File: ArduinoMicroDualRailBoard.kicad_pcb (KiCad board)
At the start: 2 copper layers, 54 parts, among them J1 Conn_01x20_Male, J2 Screw_Terminal_01x03, J3 Conn_01x20_Male, J4 Conn_01x20_Male, J5 Screw_Terminal_01x03, J6 Conn_01x20_Male, J7 SDS-50J, J8 SDS-50J, U1 L7805, U2 L7815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

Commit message: Initial PCB layout
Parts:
- moved F3 108.9 mm to (181.0, 108.6), turned to 90 degrees
- moved U8 100.3 mm to (173.4, 74.3), turned to 180 degrees
- moved R2 95.8 mm to (90.8, 125.1), turned to 270 degrees
- moved C6 92.7 mm to (203.8, 88.9), turned to 270 degrees
- moved F2 88.9 mm to (141.6, 103.6), turned to 270 degrees
- moved C7 87.2 mm to (149.2, 66.0), turned to 90 degrees
- moved C12 86.1 mm to (197.5, 88.9), turned to 270 degrees
- moved U3 85.4 mm to (203.2, 105.4), turned to 180 degrees
- moved C3 84.8 mm to (212.7, 89.5)
- moved R4 82.9 mm to (90.8, 122.6), turned to 90 degrees
- moved D5 77.9 mm to (205.7, 101.0), turned to 180 degrees
- moved U7 77.9 mm to (173.4, 101.6), turned to 180 degrees
- moved U9 77.4 mm to (212.7, 101.6), turned to 180 degrees
- moved C16 75.8 mm to (96.6, 140.3)
- moved U1 73.2 mm to (163.8, 78.1), turned to 180 degrees
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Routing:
- net (no net): vias 0 -> 5
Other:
- rule trace_min: 0.2 -> 0.16
- rule via_min_size: 0.4 -> 0.6
- board text added: "Arduino Micro MIDI Device Zach Baldwin 2020"

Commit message: PCB layout #2
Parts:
- added J9: Screw_Terminal_01x03, TerminalBlock:TerminalBlock_bornier-3_P5.08mm, F.Cu at (198.8, 140.3)
- moved R4 67.1 mm to (141.6, 78.7), turned to 0 degrees
- moved R2 63.4 mm to (134.0, 78.7), turned to 180 degrees
- moved C16 62.1 mm to (123.8, 84.5), turned to 270 degrees
- moved U5 51.5 mm to (128.9, 90.8), turned to 90 degrees
- moved D8 50.6 mm to (214.0, 120.0), turned to 180 degrees
- moved R1 49.8 mm to (215.3, 111.8), turned to 180 degrees
- moved R5 49.7 mm to (128.9, 95.2), turned to 180 degrees
- moved R3 43.1 mm to (139.1, 95.2), turned to 0 degrees
- moved D6 32.5 mm to (204.5, 114.3), turned to 270 degrees
- moved C9 29.3 mm to (169.5, 111.8)
- moved C12 29.3 mm to (178.4, 111.1)
- moved C6 29.3 mm to (184.8, 111.1)
- moved D5 29.3 mm to (186.7, 123.2)
- moved C3 29.3 mm to (193.7, 111.8)
- moved F3 29.3 mm to (161.9, 130.8)
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
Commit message: Finished routing
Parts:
- added J10: Conn_01x02_Male, Connector_PinHeader_2.54mm:PinHeader_1x02_P2.54mm_Vertical, F.Cu at (106.0, 95.2)
- moved R1 22.6 mm to (201.3, 94.0), turned to 0 degrees
- moved D8 19.9 mm to (205.1, 102.2)
- moved J4 10.3 mm to (104.1, 139.1)
- moved D1 10.2 mm to (203.8, 110.5), turned to 0 degrees
- moved D2 10.2 mm to (203.8, 86.4), turned to 0 degrees
- moved J1 10.2 mm to (104.1, 128.9)
- moved D6 9.61 mm to (214.0, 115.6), turned to 180 degrees
- moved D7 9.61 mm to (214.0, 81.3), turned to 180 degrees
- moved C14 0.64 mm to (96.6, 95.2)
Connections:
- C14 pad 2: +5V -> Net-(C14-Pad2)
- U4 pad 12: +5V -> Net-(C14-Pad2)
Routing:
- net -VDC: track 0.00 -> 128.2 mm
- net +15V: track 0.00 -> 121.5 mm, vias 0 -> 2
- net +VDC: track 0.00 -> 112.6 mm
- net -15V: track 0.00 -> 103.8 mm
- net +5V: track 0.00 -> 88.9 mm
- net /TX: track 0.00 -> 84.2 mm, vias 0 -> 1
- net /D15: track 0.00 -> 63.7 mm
- net /D16: track 0.00 -> 57.5 mm
- net /D17: track 0.00 -> 57.2 mm
- net /D21: track 0.00 -> 55.3 mm
- net /D14: track 0.00 -> 55.2 mm
- net GND: track 0.00 -> 52.7 mm
- net /D20: track 0.00 -> 49.6 mm
- net /D19: track 0.00 -> 43.8 mm
- net Net-(D9-Pad2): track 0.00 -> 38.5 mm
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- added copper zone on B.Cu, net GND
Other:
- board outline added: 135.3 x 92.7 mm
- board text added: "+15V"
- board text added: "-15V"
- board text added: "Arduino Micro"
- board text added: "Connect for normal operation"
- board text added: "D10"
- board text added: "D11"
- board text added: "D12"
- board text added: "D13"
- board text added: "D14"
- board text added: "D15"
- board text added: "D16"
- board text added: "D17"
- board text added: "D18"
- board text added: "D19"
- board text added: "D2"
- board text added: "D20"
- board text added: "D21"
- board text added: "D3"
- board text added: "D4"
- board text added: "D5"
- board text added: "D6"
- board text added: "D7"
- board text added: "D8"
- board text added: "D9"
- board text added: "GND"

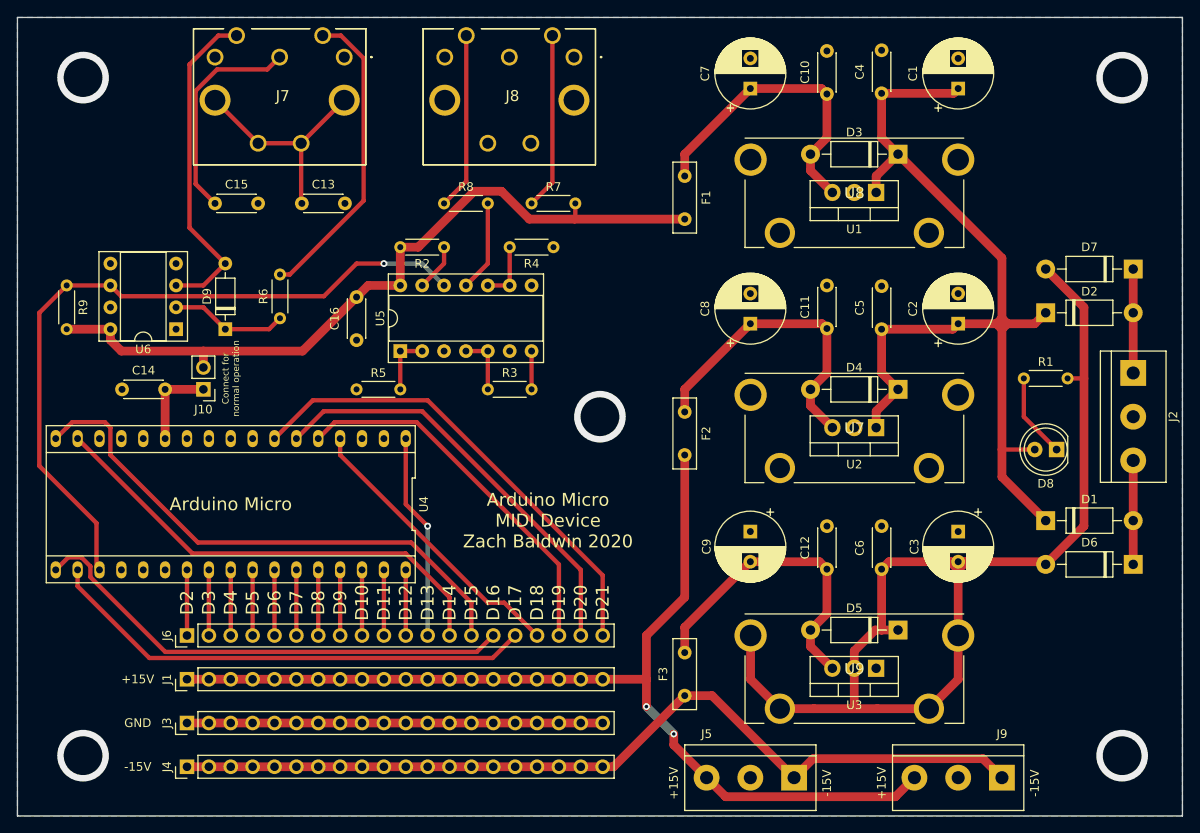
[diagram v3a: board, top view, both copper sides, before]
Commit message: Revised board layout Also: * Generated Gerbers * Added second output terminal block * Created PDF of schematic * Rendered cool RTX image of board :)
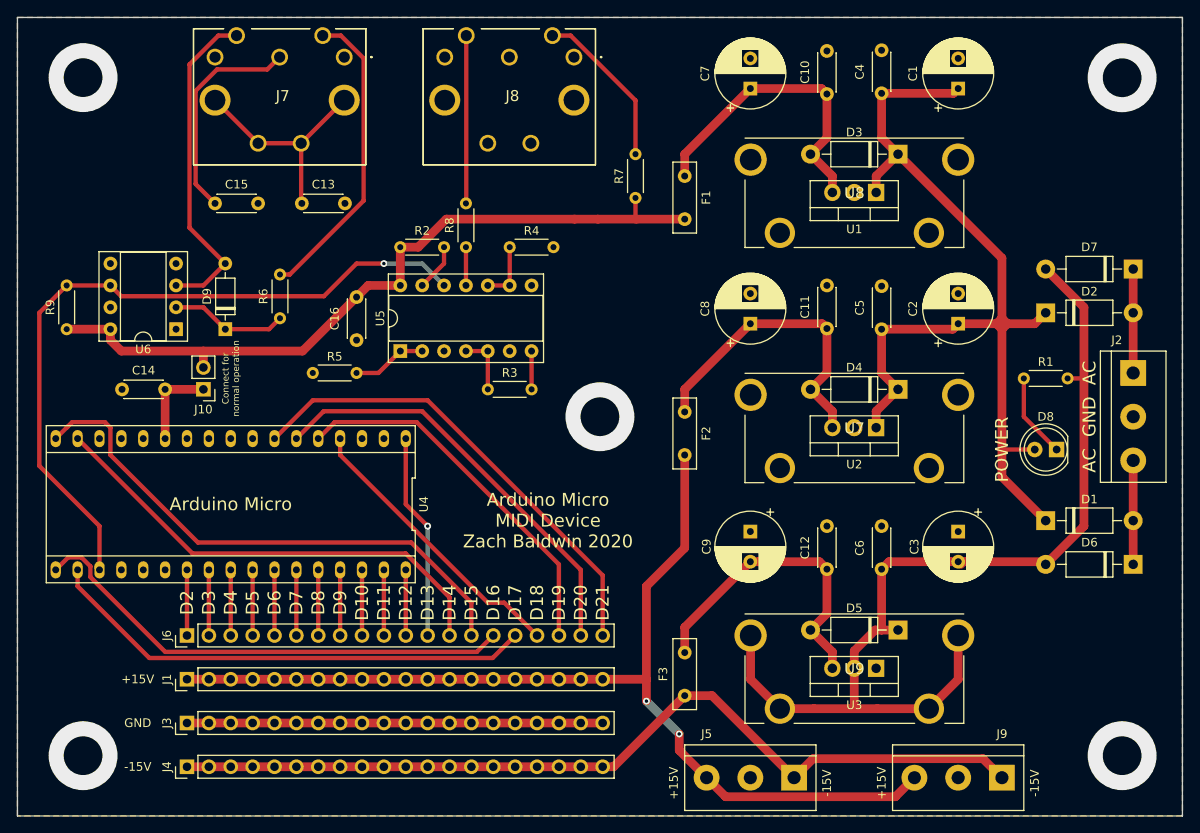
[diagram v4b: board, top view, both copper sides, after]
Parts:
- moved R7 13.4 mm to (156.2, 67.9), turned to 270 degrees
- moved R5 5.43 mm to (123.8, 93.3)
- moved R8 2.54 mm to (136.5, 73.7), turned to 270 degrees
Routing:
- net -VDC: track 128.2 -> 116.9 mm
- net Net-(R8-Pad2): track 10.6 -> 4.45 mm
- net +5V: track 88.9 -> 87.0 mm
- net Net-(R5-Pad1): track 6.98 -> 8.67 mm
- net Net-(J8-Pad4): track 20.5 -> 19.0 mm
- net Net-(J8-Pad5): track 20.6 -> 19.5 mm
- added copper zone on F.Cu, net GND
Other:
- board text added: "AC"
- board text added: "POWER"

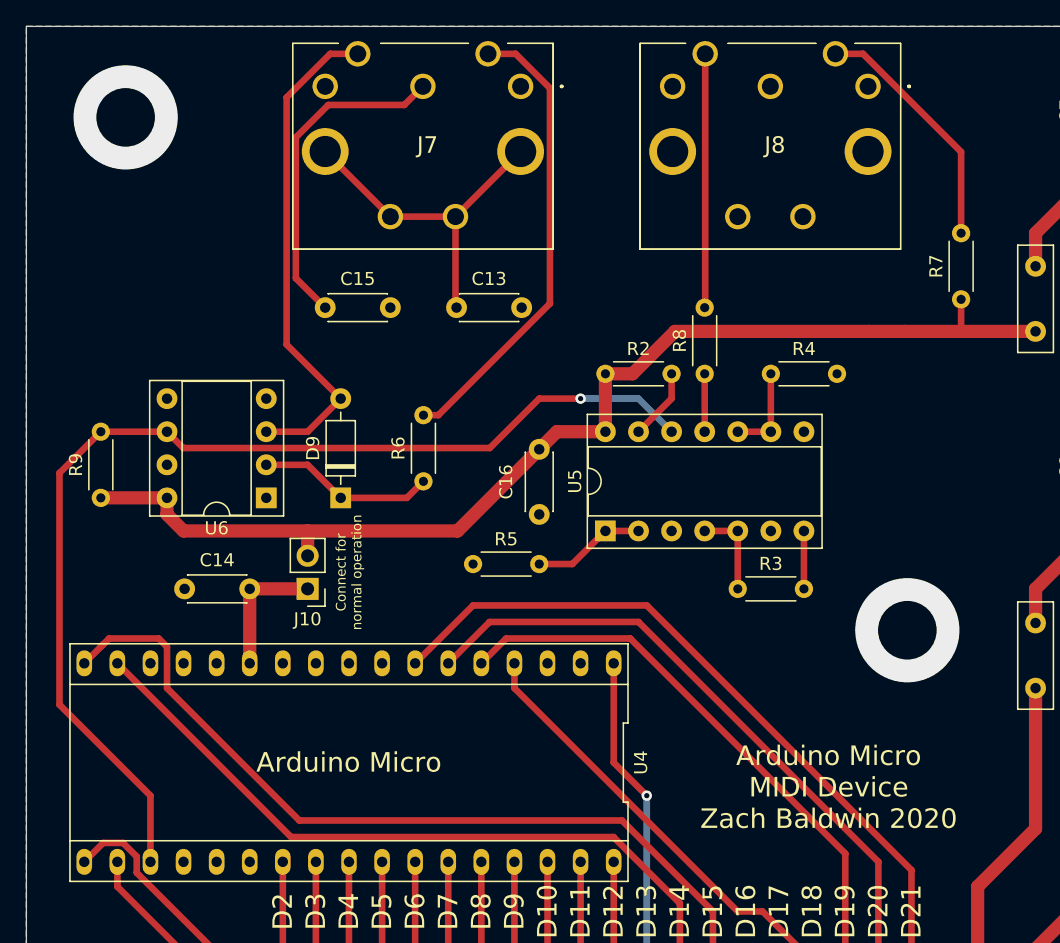
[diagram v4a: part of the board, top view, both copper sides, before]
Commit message: Updated Gerbers, fixed RX/TX reversal on Arduino
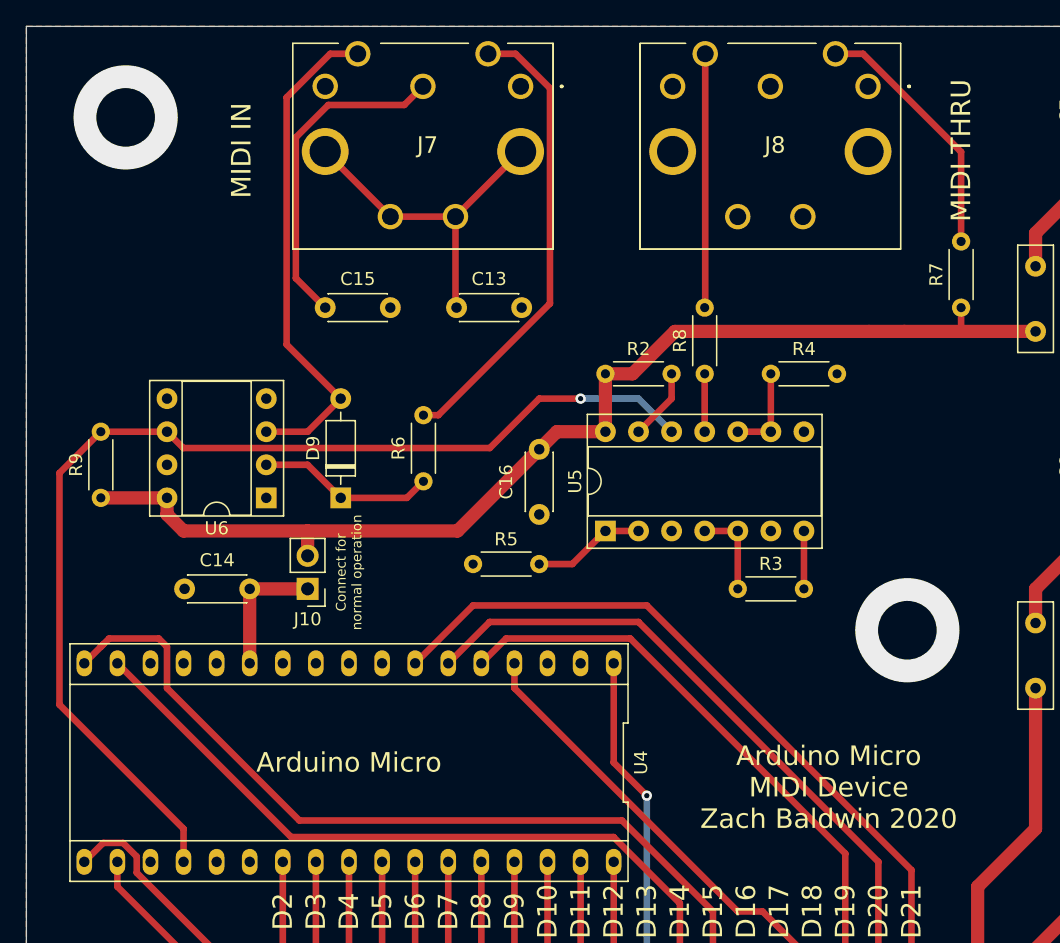
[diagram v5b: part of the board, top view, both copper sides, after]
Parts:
- moved R7 0.64 mm to (156.2, 68.6)
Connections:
- R9 pad 1: /TX -> /RX
- U5 pad 12: /TX -> /RX
- U6 pad 6: /TX -> /RX
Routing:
- net /RX: track 0.00 -> 85.2 mm, vias 0 -> 1
- net /TX: track 84.7 -> 0.49 mm, vias 1 -> 0
- net Net-(J8-Pad4): track 19.0 -> 19.6 mm
- net +5V: track 87.0 -> 86.4 mm
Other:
- board text added: "MIDI IN"
- board text added: "MIDI THRU"
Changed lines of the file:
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@@
   (general
     (thickness 1.6)
-    (drawings 39)
+    (drawings 41)
     (tracks 247)
     (zones 0)
@@
       (net 12 "Net-(D9-Pad2)"))
     (pad 6 thru_hole oval (at 7.62 5.08 180) (size 1.6 1.6) (drill 0.8) (layers *.Cu *.Mask)
-      (net 46 /TX))
+      (net 57 /RX))
     (pad 2 thru_hole oval (at 0 2.54 180) (size 1.6 1.6) (drill 0.8) (layers *.Cu *.Mask)
       (net 13 "Net-(D9-Pad1)"))
@@
       (net 47 "Net-(U5-Pad6)"))
     (pad 12 thru_hole oval (at 7.62 5.08 90) (size 1.6 1.6) (drill 0.8) (layers *.Cu *.Mask)
-      (net 46 /TX))
+      (net 57 /RX))
     (pad 5 thru_hole oval (at 0 10.16 90) (size 1.6 1.6) (drill 0.8) (layers *.Cu *.Mask)
       (net 42 "Net-(R3-Pad1)"))
@@
       (net 4 +5V))
     (pad 1 thru_hole circle (at 0 0 270) (size 1.4 1.4) (drill 0.7) (layers *.Cu *.Mask)
-      (net 46 /TX))
+      (net 57 /RX))
     (model ${KISYS3DMOD}/Resistor_THT.3dshapes/R_Axial_DIN0204_L3.6mm_D1.6mm_P5.08mm_Horizontal.wrl
       (at (xyz 0 0 0))
@@
   )
   (module Resistor_THT:R_Axial_DIN0204_L3.6mm_D1.6mm_P5.08mm_Horizontal (layer F.Cu)
-    (at 156.21 67.945 270)
+    (at 156.21 68.58 270)
     (descr "Resistor, Axial_DIN0204 series, Axial, Horizontal, pin pitch=5.08mm, 0.167W, length*diameter=3.6*1.6mm^2, http://cdn-reichelt.de/documents/datenblatt/B400/1_4W%23YAG.pdf")
     (tags "Resistor Axial_DIN0204 series Axial Horizontal pin pitch 5.08mm 0.167W length 3.6mm diameter 1.6mm")
@@
     )
   )
+  (gr_text "MIDI THRU" (at 156.21 61.595 90) (layer F.SilkS)
+    (effects (font (size 1.5 1.5) (thickness 0.3)))
+  )
+  (gr_text "MIDI IN" (at 100.965 61.595 90) (layer F.SilkS)
+    (effects (font (size 1.5 1.5) (thickness 0.3)))
+  )
   (gr_text POWER (at 198.755 102.235 90) (layer F.SilkS)
     (effects (font (size 1.5 1.5) (thickness 0.3)))
@@
   (segment (start 130.988842 78.74) (end 134.243842 75.485) (width 1.016) (layer F.Cu) (net 4))
   (segment (start 151.845 75.485) (end 149.145 75.485) (width 1.016) (layer F.Cu) (net 4))
-  (segment (start 156.21 75.405) (end 156.29 75.485) (width 0.508) (layer F.Cu) (net 4))
-  (segment (start 156.21 73.025) (end 156.21 75.405) (width 0.508) (layer F.Cu) (net 4))
   (segment (start 161.925 75.485) (end 156.29 75.485) (width 1.016) (layer F.Cu) (net 4))
   (segment (start 156.29 75.485) (end 151.845 75.485) (width 1.016) (layer F.Cu) (net 4))
+  (segment (start 156.21 75.405) (end 156.29 75.485) (width 0.508) (layer F.Cu) (net 4))
+  (segment (start 156.21 73.66) (end 156.21 75.405) (width 0.508) (layer F.Cu) (net 4))
   (segment (start 186.386999 142.543001) (end 188.595 140.335) (width 1.016) (layer F.Cu) (net 5))
   (segment (start 166.673001 142.543001) (end 186.386999 142.543001) (width 1.016) (layer F.Cu) (net 5))
@@
   (segment (start 136.565 73.62) (end 136.525 73.66) (width 0.508) (layer F.Cu) (net 37))
   (segment (start 136.565 54.175) (end 136.565 73.62) (width 0.508) (layer F.Cu) (net 37))
-  (segment (start 156.21 61.705078) (end 148.679922 54.175) (width 0.508) (layer F.Cu) (net 38))
   (segment (start 148.679922 54.175) (end 146.565 54.175) (width 0.508) (layer F.Cu) (net 38))
-  (segment (start 156.21 67.945) (end 156.21 61.705078) (width 0.508) (layer F.Cu) (net 38))
+  (segment (start 156.21 68.58) (end 156.21 61.705078) (width 0.508) (layer F.Cu) (net 38))
+  (segment (start 156.21 61.705078) (end 148.679922 54.175) (width 0.508) (layer F.Cu) (net 38))
   (segment (start 133.985 80.645) (end 131.445 83.185) (width 0.508) (layer F.Cu) (net 41))
   (segment (start 133.985 78.74) (end 133.985 80.645) (width 0.508) (layer F.Cu) (net 41))
@@
   (segment (start 123.825 93.345) (end 126.365 93.345) (width 0.508) (layer F.Cu) (net 44))
   (segment (start 136.525 78.74) (end 136.525 83.185) (width 0.508) (layer F.Cu) (net 45))
-  (segment (start 90.17 83.185) (end 95.25 83.185) (width 0.508) (layer F.Cu) (net 46))
-  (segment (start 96.504001 84.439001) (end 120.030999 84.439001) (width 0.508) (layer F.Cu) (net 46))
-  (segment (start 95.25 83.185) (end 96.504001 84.439001) (width 0.508) (layer F.Cu) (net 46))
-  (via (at 127 80.645) (size 0.8) (drill 0.4) (layers F.Cu B.Cu) (net 46))
-  (segment (start 120.030999 84.439001) (end 123.825 80.645) (width 0.508) (layer F.Cu) (net 46))
-  (segment (start 123.825 80.645) (end 127 80.645) (width 0.508) (layer F.Cu) (net 46))
-  (segment (start 131.445 80.645) (end 133.985 83.185) (width 0.508) (layer B.Cu) (net 46))
-  (segment (start 127 80.645) (end 131.445 80.645) (width 0.508) (layer B.Cu) (net 46))
+  (segment (start 90.17 83.185) (end 95.25 83.185) (width 0.508) (layer F.Cu) (net 57))
+  (segment (start 96.504001 84.439001) (end 120.030999 84.439001) (width 0.508) (layer F.Cu) (net 57))
+  (segment (start 95.25 83.185) (end 96.504001 84.439001) (width 0.508) (layer F.Cu) (net 57))
+  (via (at 127 80.645) (size 0.8) (drill 0.4) (layers F.Cu B.Cu) (net 57))
+  (segment (start 120.030999 84.439001) (end 123.825 80.645) (width 0.508) (layer F.Cu) (net 57))
+  (segment (start 123.825 80.645) (end 127 80.645) (width 0.508) (layer F.Cu) (net 57))
+  (segment (start 131.445 80.645) (end 133.985 83.185) (width 0.508) (layer B.Cu) (net 57))
+  (segment (start 127 80.645) (end 131.445 80.645) (width 0.508) (layer B.Cu) (net 57))
   (segment (start 93.98 116.205) (end 93.634 115.859) (width 0.508) (layer F.Cu) (net 46))
-  (segment (start 86.995 104.14) (end 86.995 86.36) (width 0.508) (layer F.Cu) (net 46))
-  (segment (start 93.98 116.205) (end 93.98 111.125) (width 0.508) (layer F.Cu) (net 46))
-  (segment (start 86.995 86.36) (end 90.17 83.185) (width 0.508) (layer F.Cu) (net 46))
-  (segment (start 93.98 111.125) (end 86.995 104.14) (width 0.508) (layer F.Cu) (net 46))
   (segment (start 161.925 67.945) (end 169.545 60.325) (width 1.016) (layer F.Cu) (net 53))
   (segment (start 161.925 70.485) (end 161.925 67.945) (width 1.016) (layer F.Cu) (net 53))
@@
   (segment (start 168.755 116.05) (end 169.545 115.26) (width 1.016) (layer F.Cu) (net 55))
   (segment (start 170.505 115.26) (end 177.57 115.26) (width 1.016) (layer F.Cu) (net 55))
+  (segment (start 86.995 86.36) (end 90.17 83.185) (width 0.508) (layer F.Cu) (net 57))
+  (segment (start 96.52 116.205) (end 96.52 113.665) (width 0.508) (layer F.Cu) (net 57))
+  (segment (start 86.995 104.14) (end 86.995 86.36) (width 0.508) (layer F.Cu) (net 57))
+  (segment (start 96.52 113.665) (end 86.995 104.14) (width 0.508) (layer F.Cu) (net 57))
   (segment (start 101.6 95.885) (end 101.6 100.965) (width 1.016) (layer F.Cu) (net 66))
   (segment (start 106.045 95.25) (end 101.6 95.25) (width 1.016) (layer F.Cu) (net 66))
